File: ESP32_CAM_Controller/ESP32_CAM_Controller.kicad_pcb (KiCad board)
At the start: 2 copper layers, 61.8 x 86 mm, 24 parts, among them J1 Conn_01x03, J10 Volt_Sel, J2 Conn_01x03, J3 Conn_01x03, J4 Conn_01x03, U1 ESP32-CAM, U2 LM7805_TO220, U3 SN74HCT245N

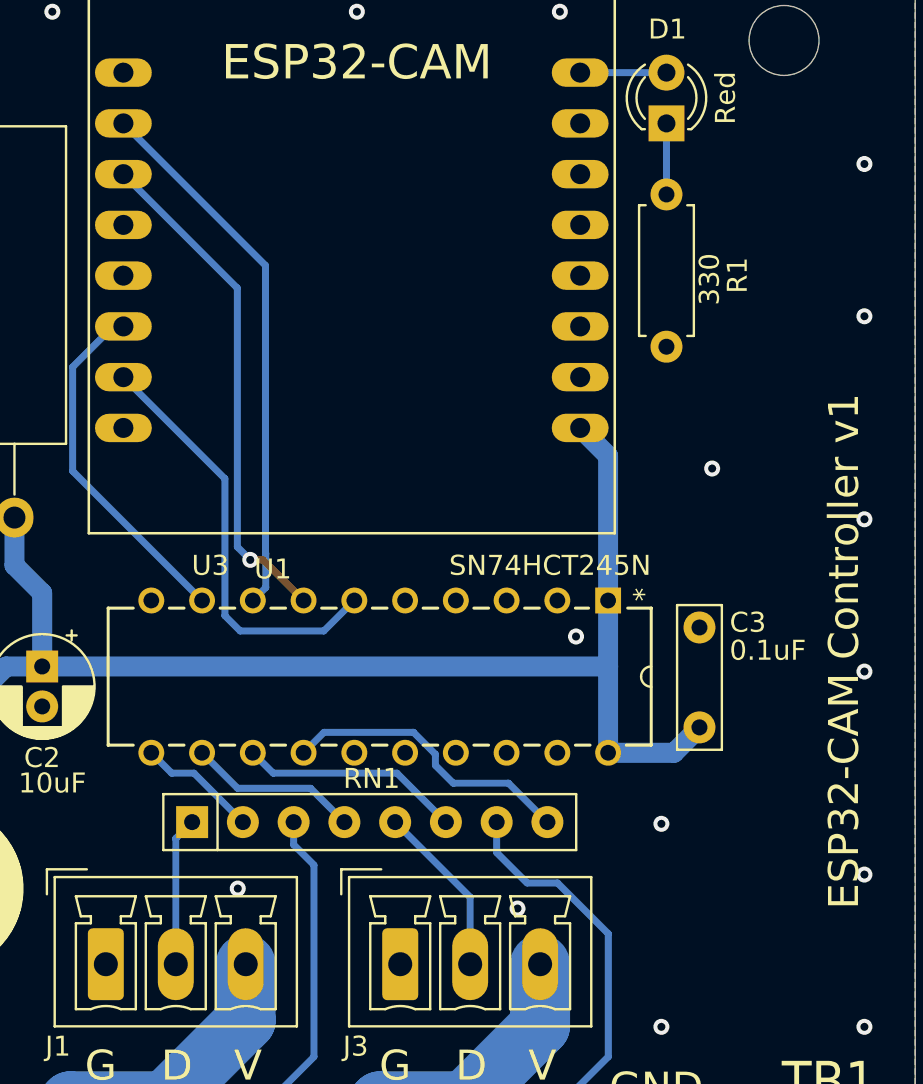
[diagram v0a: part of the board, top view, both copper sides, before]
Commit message: added kicad logo
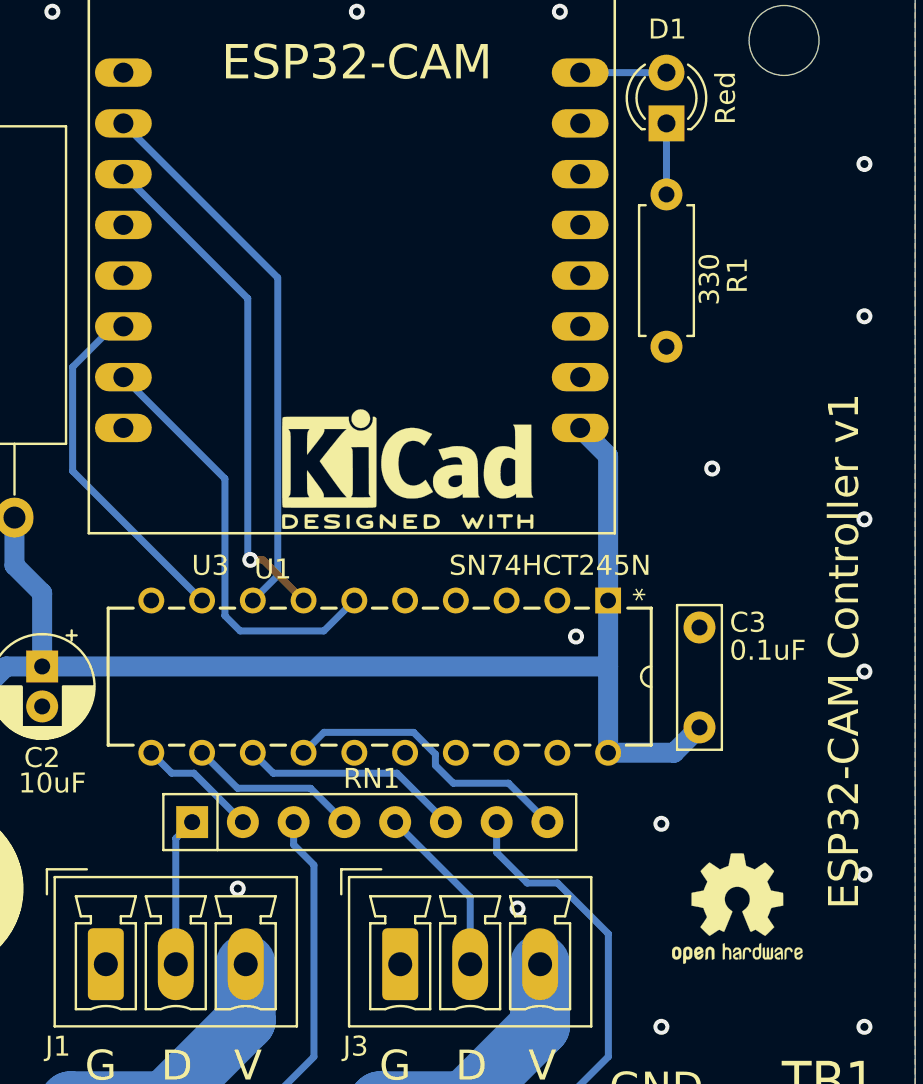
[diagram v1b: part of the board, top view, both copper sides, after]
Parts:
- added REF**: KiCad-Logo2_5mm_SilkScreen, Symbol:KiCad-Logo2_5mm_SilkScreen, F.Cu at (151.8, 72.8)
- added REF**: OSHW-Logo2_7.3x6mm_SilkScreen, Symbol:OSHW-Logo2_7.3x6mm_SilkScreen, F.Cu at (168.2, 94.8)
